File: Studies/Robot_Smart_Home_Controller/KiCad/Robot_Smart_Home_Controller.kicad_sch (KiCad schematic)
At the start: 5 parts, among them SW1 SW_Push_SPDT, SW2 SW_Push_SPDT, SW3 SW_Push_SPDT, SW4 SW_Push_SPDT, SW5 SW_Push_SPDT

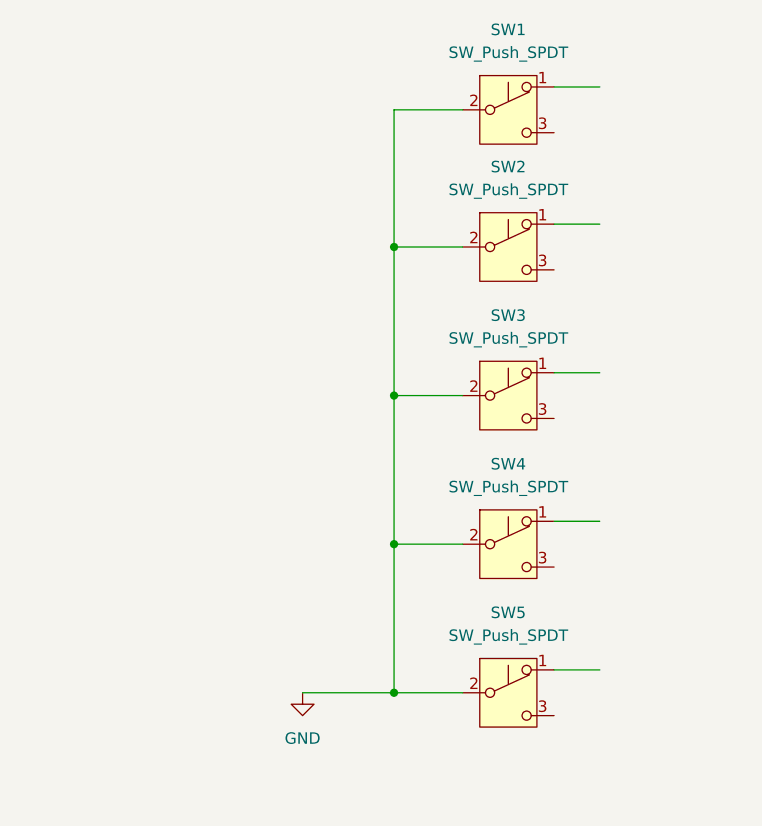
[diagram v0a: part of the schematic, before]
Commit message: Adding updated schematic - switches and resistors added.
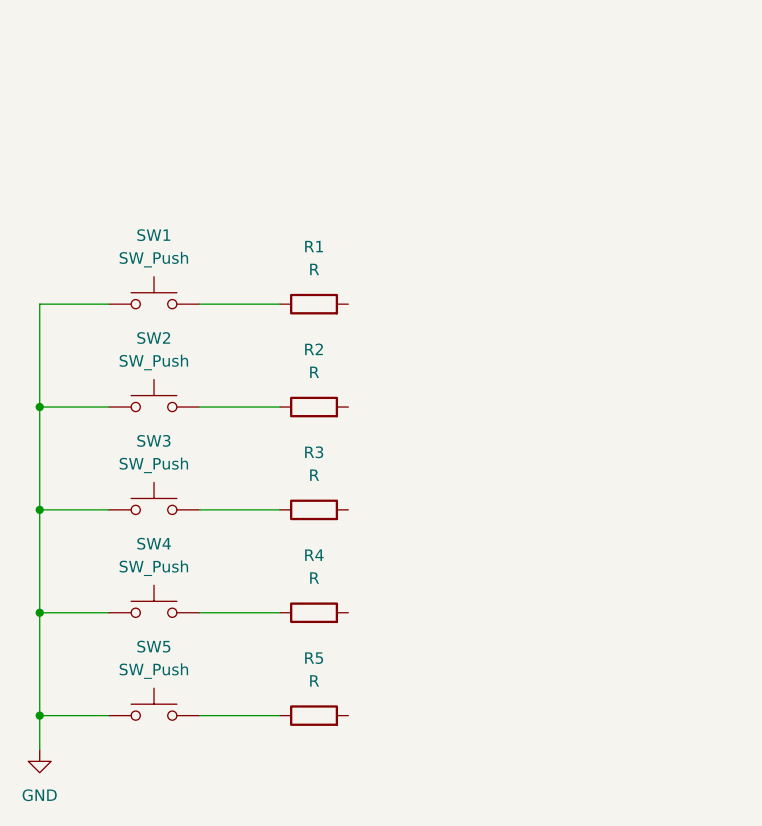
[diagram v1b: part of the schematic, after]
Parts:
- removed SW1, SW2, SW3, SW4, SW5: SW_Push_SPDT, symbol Switch:SW_Push_SPDT
- added R1, R2, R3, R4, R5: R, symbol Device:R
- added SW1, SW2, SW3, SW4, SW5: SW_Push, symbol Switch:SW_Push
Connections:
- net GND: now also SW1.1, SW2.1, SW3.1, SW4.1, SW5.1
- new net: R3.1, SW3.2
- new net: R5.1, SW5.2
- new net: R1.1, SW1.2
- new net: R4.1, SW4.2
- new net: R2.1, SW2.2

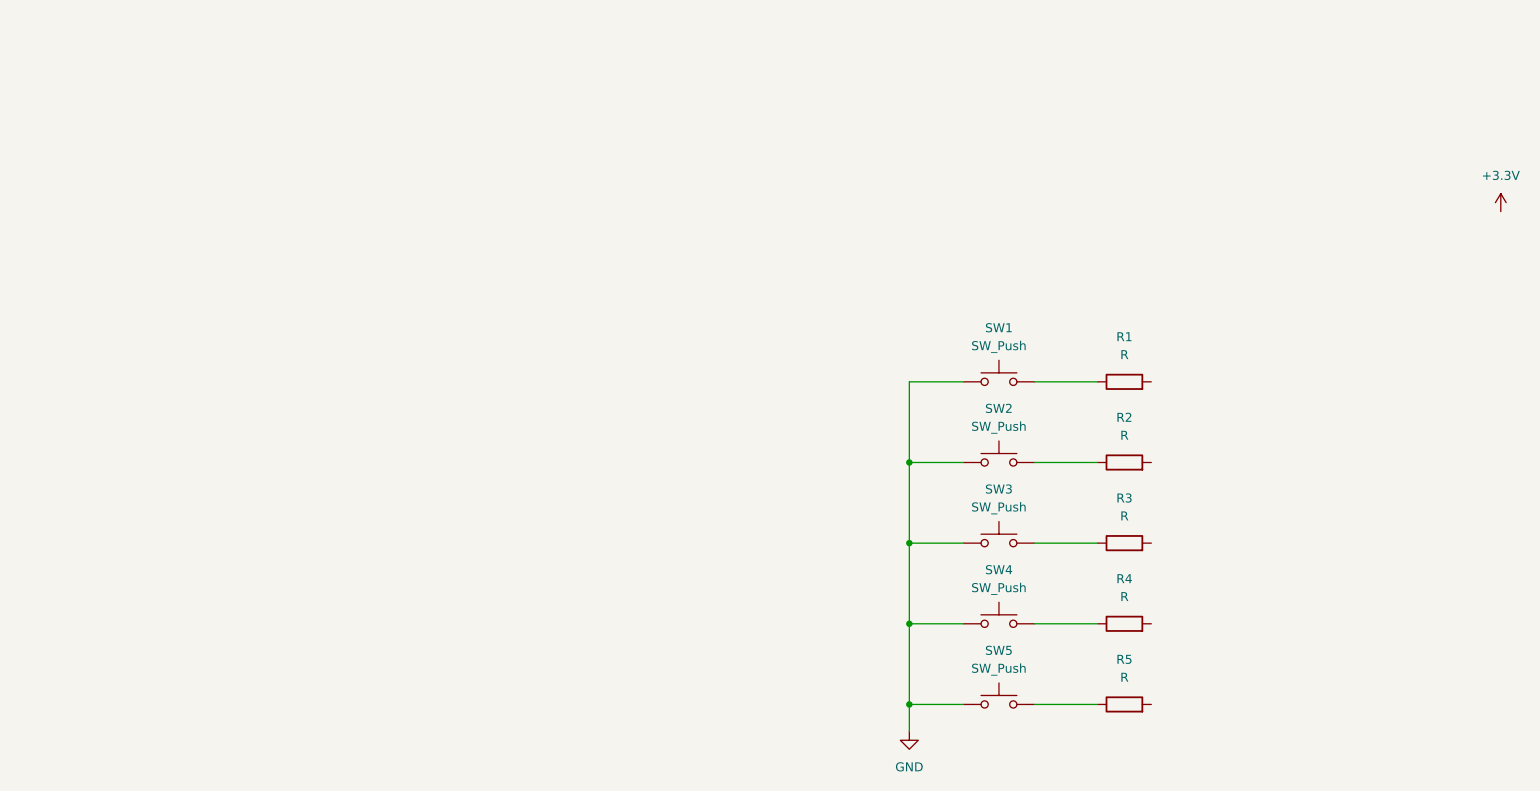
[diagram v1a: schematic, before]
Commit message: Updated schematic for Robot Smart Home Controller
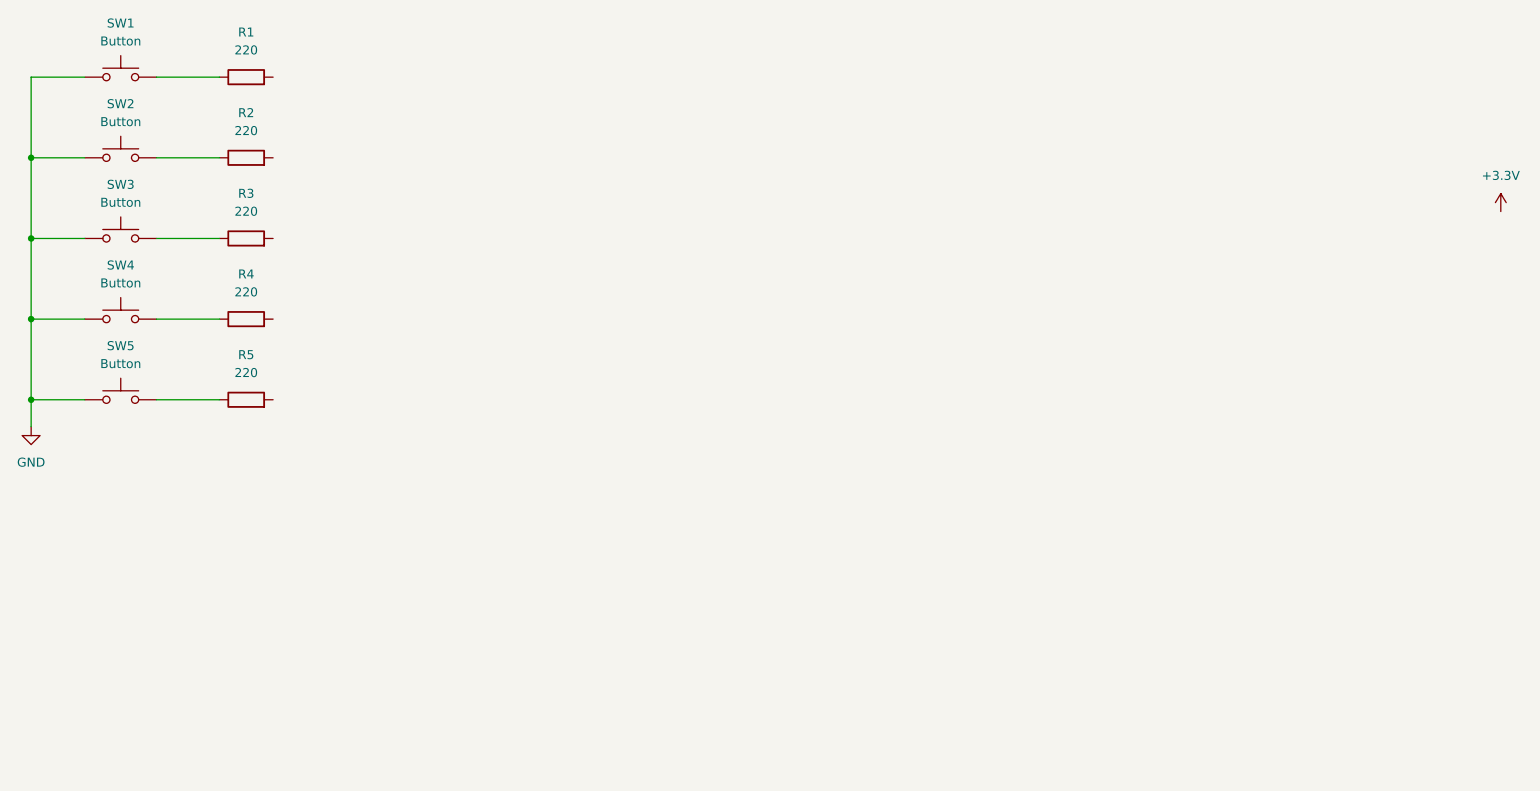
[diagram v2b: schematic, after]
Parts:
- R1, R2, R3, R4, R5: value R -> 220
- SW1, SW2, SW3, SW4, SW5: value SW_Push -> Button
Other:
- moved on the sheet: R1, R2, R3, R4, R5, SW1, SW2, SW3, SW4, SW5
